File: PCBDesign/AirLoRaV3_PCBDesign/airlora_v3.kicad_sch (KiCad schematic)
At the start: 0 parts

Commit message: Update circiut
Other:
- sheet MCU ports: added PA4, PA5, PA6, PA7; removed 3.3V
- sheet Power ports: added none; removed 3.3V, 5V
- sheet STlink ports: added none; removed 3.3V
- sheet Sensor ports: added EN_CO, EN_N02, EN_PM, EN_SHT; removed 3.3V, 5V

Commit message: Update PCB layout
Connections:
- no-connect marks 4 -> 8
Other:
- sheet MCU ports: added PA11, PA12, PA8, PB2; removed none
- sheet Power ports: added En; removed none
- sheet Sensor ports: added DHT; removed SCL_SHT21, SDA_SHT21
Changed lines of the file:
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@@
+	)
+	(no_connect
+		(at 147.32 113.03)
 	)
 	(no_connect
@@
 	)
 	(no_connect
+		(at 147.32 123.19)
+	)
+	(no_connect
+		(at 147.32 115.57)
+	)
+	(no_connect
 		(at 110.49 119.38)
 	)
 	(no_connect
+		(at 110.49 87.63)
+	)
+	(no_connect
 		(at 110.49 124.46)
 	)
 	(wire
 		(pts
+			(xy 147.32 120.65) (xy 180.34 120.65)
+		)
+		(stroke
+			(width 0)
+			(type default)
+		)
+	)
+	(wire
+		(pts
 			(xy 83.82 114.3) (xy 110.49 114.3)
 		)
@@
 	(wire
 		(pts
-			(xy 147.32 115.57) (xy 180.34 115.57)
-		)
-		(stroke
-			(width 0)
-			(type default)
-		)
-	)
-	(wire
-		(pts
 			(xy 83.82 116.84) (xy 110.49 116.84)
 		)
@@
 	(wire
 		(pts
+			(xy 95.25 76.2) (xy 95.25 85.09)
+		)
+		(stroke
+			(width 0)
+			(type default)
+		)
+	)
+	(wire
+		(pts
+			(xy 95.25 85.09) (xy 110.49 85.09)
+		)
+		(stroke
+			(width 0)
+			(type default)
+		)
+	)
+	(wire
+		(pts
 			(xy 147.32 118.11) (xy 180.34 118.11)
 		)
@@
 	(wire
 		(pts
+			(xy 83.82 76.2) (xy 95.25 76.2)
+		)
+		(stroke
+			(width 0)
+			(type default)
+		)
+	)
+	(wire
+		(pts
 			(xy 147.32 92.71) (xy 180.34 92.71)
 		)
@@
 		(pts
 			(xy 147.32 86.36) (xy 180.34 86.36)
-		)
-		(stroke
-			(width 0)
-			(type default)
-		)
-	)
-	(wire
-		(pts
-			(xy 147.32 113.03) (xy 180.34 113.03)
 		)
 		(stroke
@@
 			)
 		)
-		(pin "SCL_SHT21" input
-			(at 180.34 113.03 180)
-			(effects
-				(font
-					(size 1.27 1.27)
-				)
-				(justify left)
-			)
-		)
-		(pin "SDA_SHT21" input
-			(at 180.34 115.57 180)
-			(effects
-				(font
-					(size 1.27 1.27)
-				)
-				(justify left)
-			)
-		)
 		(pin "TX_NO2" input
 			(at 180.34 83.82 180)
@@
 		(pin "EN_SHT" input
 			(at 180.34 118.11 180)
+			(effects
+				(font
+					(size 1.27 1.27)
+				)
+				(justify left)
+			)
+		)
+		(pin "DHT" input
+			(at 180.34 120.65 180)
 			(effects
 				(font
@@
 			)
 		)
+		(pin "En" input
+			(at 83.82 76.2 0)
+			(effects
+				(font
+					(size 1.27 1.27)
+				)
+				(justify right)
+			)
+		)
 		(instances
 			(project "airlora-kicad"
@@
 		)
 		(pin "PA4" input
-			(at 147.32 86.36 0)
-			(effects
-				(font
-					(size 1.27 1.27)
-				)
-				(justify right)
+			(at 110.49 87.63 180)
+			(effects
+				(font
+					(size 1.27 1.27)
+				)
+				(justify left)
 			)
 		)
@@
 		)
 		(pin "PA7" input
+			(at 147.32 123.19 0)
+			(effects
+				(font
+					(size 1.27 1.27)
+				)
+				(justify right)
+			)
+		)
+		(pin "PA8" input
+			(at 147.32 86.36 0)
+			(effects
+				(font
+					(size 1.27 1.27)
+				)
+				(justify right)
+			)
+		)
+		(pin "PA12" input
+			(at 110.49 85.09 180)
+			(effects
+				(font
+					(size 1.27 1.27)
+				)
+				(justify left)
+			)
+		)
+		(pin "PB2" input
 			(at 147.32 118.11 0)
 			(effects
 				(font
+					(size 1.27 1.27)
+				)
+				(justify right)
+			)
+		)
+		(pin "PA11" input
+			(at 147.32 120.65 0)
+			(effects
+				(font

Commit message: Update schematic
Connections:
- no-connect marks 8 -> 0
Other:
- added sheet MCU Sub (MCU Sub.kicad_sch)
- sheet MCU ports: added SCL1, SDA1; removed PA10_RX, PA11, PA12, PA2_TX, PA3_RX, PA4, PA5, PA6, PA7, PA8, PA9_TX, PB13_SCL, PB14_SDA, PB2, PB8_SCL, PB9_SDA, T_JTDI, T_SWO, T_VCP_RX, T_VCP_TX
- sheet STlink ports: added T_SWCLK1, T_SWDIO1; removed none

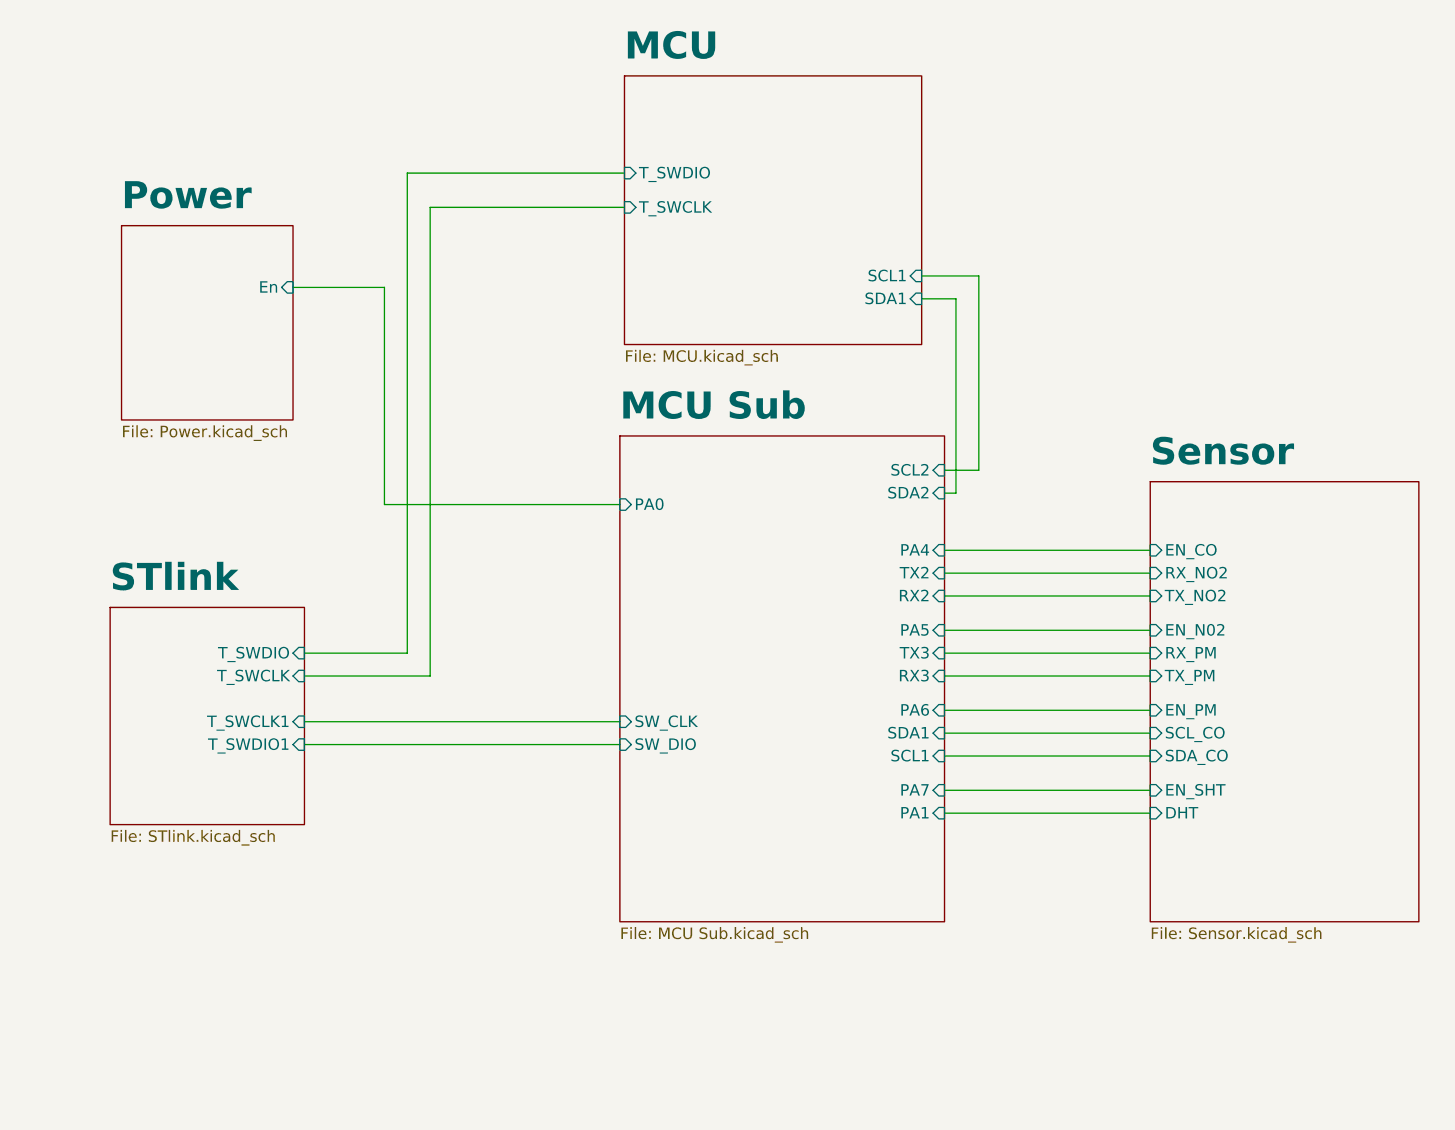
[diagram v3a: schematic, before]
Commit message: Update circuit buck converter and sensor
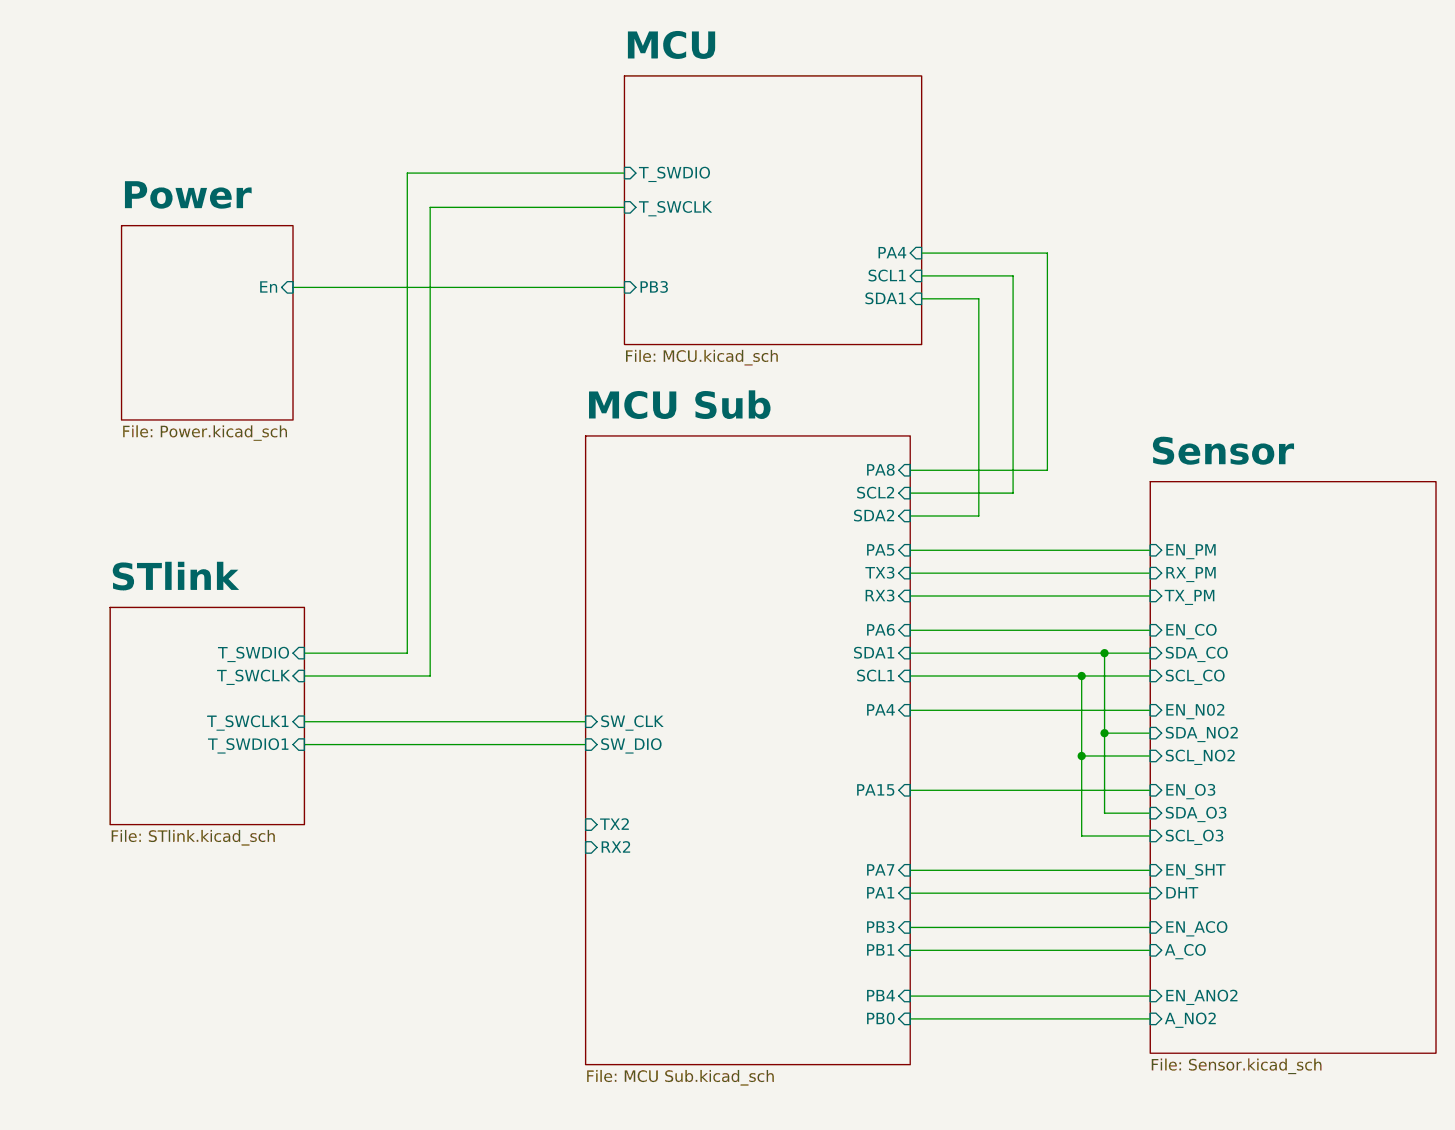
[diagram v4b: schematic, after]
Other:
- sheet MCU ports: added PA4, PB3; removed none
- sheet MCU Sub ports: added PA15, PA8, PB0, PB1, PB3, PB4; removed PA0
- sheet Sensor ports: added A_CO, A_NO2, EN_ACO, EN_ANO2, EN_O3, SCL_NO2, SCL_O3, SDA_NO2, SDA_O3; removed RX_NO2, TX_NO2

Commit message: Update schematic
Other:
- sheet MCU ports: added SCL2, SDA2; removed SCL1, SDA1
- sheet Sensor ports: added SCL_SHT, SDA_SHT; removed DHT
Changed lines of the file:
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@@
+	)
+	(junction
+		(at 185.42 125.73)
+		(diameter 0)
+		(color 0 0 0 0)
 	)
 	(junction
@@
 	)
 	(junction
+		(at 182.88 128.27)
+		(diameter 0)
+		(color 0 0 0 0)
+	)
+	(junction
 		(at 185.42 107.95)
 		(diameter 0)
@@
 	(wire
 		(pts
-			(xy 163.83 148.59) (xy 190.5 148.59)
+			(xy 163.83 152.4) (xy 190.5 152.4)
 		)
 		(stroke
@@
 	(wire
 		(pts
-			(xy 163.83 140.97) (xy 190.5 140.97)
+			(xy 163.83 144.78) (xy 190.5 144.78)
 		)
 		(stroke
@@
 	(wire
 		(pts
+			(xy 190.5 134.62) (xy 185.42 134.62)
+		)
+		(stroke
+			(width 0)
+			(type default)
+		)
+	)
+	(wire
+		(pts
 			(xy 165.1 68.58) (xy 171.45 68.58)
 		)
@@
 	(wire
 		(pts
+			(xy 182.88 137.16) (xy 182.88 128.27)
+		)
+		(stroke
+			(width 0)
+			(type default)
+		)
+	)
+	(wire
+		(pts
 			(xy 163.83 96.52) (xy 190.5 96.52)
 		)
@@
 	(wire
 		(pts
-			(xy 163.83 146.05) (xy 190.5 146.05)
-		)
-		(stroke
-			(width 0)
-			(type default)
-		)
-	)
-	(wire
-		(pts
-			(xy 163.83 134.62) (xy 190.5 134.62)
+			(xy 163.83 149.86) (xy 190.5 149.86)
+		)
+		(stroke
+			(width 0)
+			(type default)
+		)
+	)
+	(wire
+		(pts
+			(xy 190.5 137.16) (xy 182.88 137.16)
 		)
 		(stroke
@@
 	(wire
 		(pts
-			(xy 163.83 138.43) (xy 190.5 138.43)
+			(xy 163.83 142.24) (xy 190.5 142.24)
 		)
 		(stroke
@@
 		(pts
 			(xy 185.42 125.73) (xy 185.42 116.84)
+		)
+		(stroke
+			(width 0)
+			(type default)
+		)
+	)
+	(wire
+		(pts
+			(xy 185.42 134.62) (xy 185.42 125.73)
 		)
 		(stroke
@@
 	(sheet
 		(at 190.5 88.9)
-		(size 31.75 63.5)
+		(size 31.75 67.31)
 		(fields_autoplaced yes)
 		(stroke
@@
 		)
 		(property "Sheetfile" "Sensor.kicad_sch"
-			(at 190.5 152.9846 0)
+			(at 190.5 156.7946 0)
 			(effects
 				(font
@@
 			)
 		)
-		(pin "DHT" input
-			(at 190.5 134.62 180)
-			(effects
-				(font
-					(size 1.27 1.27)
-				)
-				(justify left)
-			)
-		)
 		(pin "SDA_O3" input
 			(at 190.5 125.73 180)
@@
 		)
 		(pin "A_CO" input
-			(at 190.5 140.97 180)
+			(at 190.5 144.78 180)
 			(effects
 				(font
@@
 		)
 		(pin "EN_ACO" input
-			(at 190.5 138.43 180)
+			(at 190.5 142.24 180)
 			(effects
 				(font
@@
 		)
 		(pin "EN_ANO2" input
-			(at 190.5 146.05 180)
+			(at 190.5 149.86 180)
 			(effects
 				(font
@@
 		)
 		(pin "A_NO2" input
-			(at 190.5 148.59 180)
+			(at 190.5 152.4 180)
+			(effects
+				(font
+					(size 1.27 1.27)
+				)
+				(justify left)
+			)
+		)
+		(pin "SCL_SHT" input
+			(at 190.5 137.16 180)
+			(effects
+				(font
+					(size 1.27 1.27)
+				)
+				(justify left)
+			)
+		)
+		(pin "SDA_SHT" input
+			(at 190.5 134.62 180)
 			(effects
 				(font
@@
 			)
 		)
-		(pin "SCL1" input
+		(pin "SCL2" input
 			(at 165.1 66.04 0)
 			(effects
@@
 			)
 		)
-		(pin "SDA1" input
+		(pin "SDA2" input
 			(at 165.1 68.58 0)
 			(effects
@@
 	(sheet
 		(at 127.762 83.82)
-		(size 36.068 69.85)
+		(size 36.068 72.39)
 		(fields_autoplaced yes)
 		(stroke
@@
 		)
 		(property "Sheetfile" "MCU Sub.kicad_sch"
-			(at 127.762 154.2546 0)
+			(at 127.762 156.7946 0)
 			(effects
 				(font
@@
 		)
 		(pin "PB1" input
-			(at 163.83 140.97 0)
+			(at 163.83 144.78 0)
 			(effects
 				(font
@@
 		)
 		(pin "PB0" input
-			(at 163.83 148.59 0)
+			(at 163.83 152.4 0)
 			(effects
 				(font
@@
 		)
 		(pin "PB3" input
-			(at 163.83 138.43 0)
+			(at 163.83 142.24 0)
 			(effects
 				(font
@@
 		)
 		(pin "PB4" input
-			(at 163.83 146.05 0)
-			(effects
-				(font
+			(at 163.83 149.86 0)
+			(effects
+				(font
